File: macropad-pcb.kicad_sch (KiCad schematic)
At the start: 25 parts, among them J1 Conn_01x01_Socket, J10 Conn_01x01_Socket, J2 Conn_01x01_Socket, J3 Conn_01x01_Socket, J4 Conn_01x01_Socket, J5 Conn_01x01_Socket, J6 Conn_01x01_Socket, J7 Conn_01x01_Socket, J8 Conn_01x01_Socket, J9 Conn_01x01_Socket

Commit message: updated w. flipped main connectior
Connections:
- net GND: now also MAIN1.1, MAIN1.2, MAIN1.3, MAIN1.4; no longer MAIN1.13, MAIN1.14, MAIN1.15, MAIN1.16
- net LED_DI: now also MAIN1.6; no longer MAIN1.11
- net LED_DO_MACRO: now also MAIN1.5; no longer MAIN1.12
- net VCC: now also MAIN1.13, MAIN1.14, MAIN1.15, MAIN1.16; no longer MAIN1.1, MAIN1.2, MAIN1.3, MAIN1.4
- net col10: now also MAIN1.10; no longer MAIN1.7
- net col11: now also MAIN1.9; no longer MAIN1.8
- net col8: now also MAIN1.12; no longer MAIN1.5
- net col9: now also MAIN1.11; no longer MAIN1.6
- net row8: now also MAIN1.8; no longer MAIN1.9
- net row9: now also MAIN1.7; no longer MAIN1.10

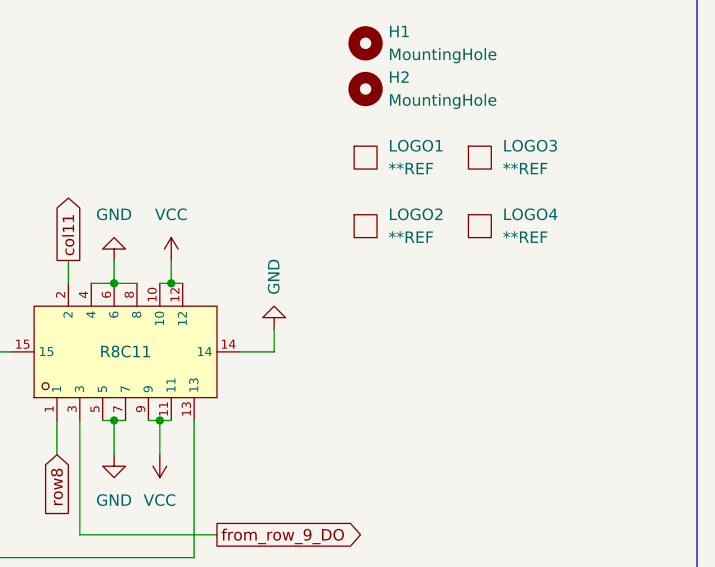
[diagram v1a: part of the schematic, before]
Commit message: added cyboard logo
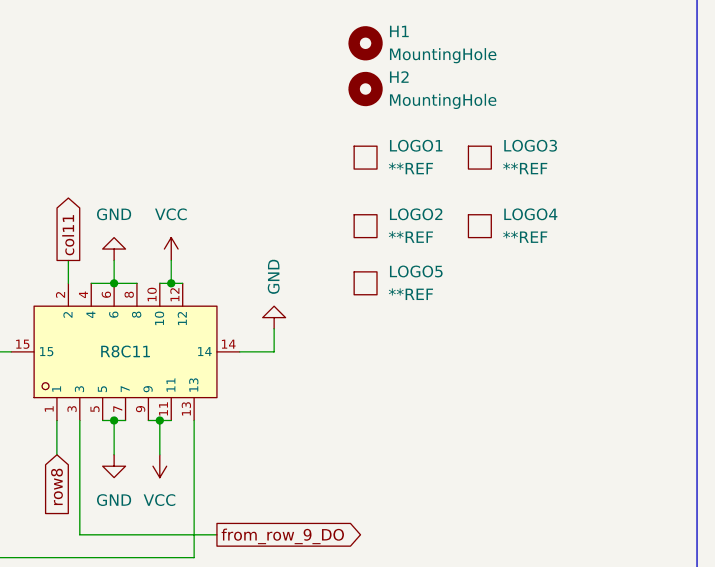
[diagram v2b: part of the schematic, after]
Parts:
- added LOGO5: **REF, ct-kicad:cyboard-logo-10mm, symbol ct-kicad:cyboard-logo-10mm
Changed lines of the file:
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@@
+    )
+  )
+  (symbol (lib_id "ct-kicad:cyboard-logo-10mm") (at 240.03 72.39 0) (unit 1)
+    (in_bom no) (on_board yes) (dnp no) (fields_autoplaced)
+    (property "Reference" "LOGO5" (at 242.57 71.12 0)
+      (effects (font (size 1.27 1.27)) (justify left))
+    )
+    (property "Value" "**REF" (at 242.57 73.66 0)
+      (effects (font (size 1.27 1.27)) (justify left))
+    )
+    (property "Footprint" "ct-kicad:cyboard-logo-10mm" (at 240.03 72.39 0)
+      (effects (font (size 1.27 1.27)) hide)
+    )
+    (property "Datasheet" "" (at 240.03 72.39 0)
+      (effects (font (size 1.27 1.27)) hide)
+    )
+    (instances
+      (project "macropad-pcb"
+        (path "/a1d63ebf-3d6e-4f37-a8f0-07094ad9e2ad"
+          (reference "LOGO5") (unit 1)
+        )
+      )
     )
   )

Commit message: added cyboard logo, placed order
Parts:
- H1, H2, J1, J2, J3, J4, J5, J6, J7, J8: now left out of the parts list
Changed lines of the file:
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@@
   )
   (symbol (lib_id "Connector:Conn_01x01_Socket") (at 30.48 142.24 180) (unit 1)
-    (in_bom yes) (on_board yes) (dnp no) (fields_autoplaced)
+    (in_bom no) (on_board yes) (dnp no) (fields_autoplaced)
     (property "Reference" "J3" (at 31.115 137.16 0)
       (effects (font (size 1.27 1.27)))
@@
   )
   (symbol (lib_id "Connector:Conn_01x01_Socket") (at 30.48 134.62 180) (unit 1)
-    (in_bom yes) (on_board yes) (dnp no) (fields_autoplaced)
+    (in_bom no) (on_board yes) (dnp no) (fields_autoplaced)
     (property "Reference" "J2" (at 31.115 129.54 0)
       (effects (font (size 1.27 1.27)))
@@
   )
   (symbol (lib_id "Mechanical:MountingHole") (at 240.03 50.8 0) (unit 1)
-    (in_bom yes) (on_board yes) (dnp no) (fields_autoplaced)
+    (in_bom no) (on_board yes) (dnp no) (fields_autoplaced)
     (property "Reference" "H2" (at 242.57 49.53 0)
       (effects (font (size 1.27 1.27)) (justify left))
@@
   )
   (symbol (lib_id "Connector:Conn_01x01_Socket") (at 57.15 128.27 180) (unit 1)
-    (in_bom yes) (on_board yes) (dnp no) (fields_autoplaced)
+    (in_bom no) (on_board yes) (dnp no) (fields_autoplaced)
     (property "Reference" "J5" (at 57.785 123.19 0)
       (effects (font (size 1.27 1.27)))
@@
   )
   (symbol (lib_id "Connector:Conn_01x01_Socket") (at 57.15 135.89 180) (unit 1)
-    (in_bom yes) (on_board yes) (dnp no) (fields_autoplaced)
+    (in_bom no) (on_board yes) (dnp no) (fields_autoplaced)
     (property "Reference" "J6" (at 57.785 130.81 0)
       (effects (font (size 1.27 1.27)))
@@
   )
   (symbol (lib_id "Connector:Conn_01x01_Socket") (at 57.15 151.13 180) (unit 1)
-    (in_bom yes) (on_board yes) (dnp no) (fields_autoplaced)
+    (in_bom no) (on_board yes) (dnp no) (fields_autoplaced)
     (property "Reference" "J8" (at 57.785 146.05 0)
       (effects (font (size 1.27 1.27)))
@@
   )
   (symbol (lib_id "Mechanical:MountingHole") (at 240.03 45.72 0) (unit 1)
-    (in_bom yes) (on_board yes) (dnp no) (fields_autoplaced)
+    (in_bom no) (on_board yes) (dnp no) (fields_autoplaced)
     (property "Reference" "H1" (at 242.57 44.45 0)
       (effects (font (size 1.27 1.27)) (justify left))
@@
   )
   (symbol (lib_id "Connector:Conn_01x01_Socket") (at 30.48 149.86 180) (unit 1)
-    (in_bom yes) (on_board yes) (dnp no) (fields_autoplaced)
+    (in_bom no) (on_board yes) (dnp no) (fields_autoplaced)
     (property "Reference" "J4" (at 31.115 144.78 0)
       (effects (font (size 1.27 1.27)))
@@
   )
   (symbol (lib_id "Connector:Conn_01x01_Socket") (at 57.15 143.51 180) (unit 1)
-    (in_bom yes) (on_board yes) (dnp no) (fields_autoplaced)
+    (in_bom no) (on_board yes) (dnp no) (fields_autoplaced)
     (property "Reference" "J7" (at 57.785 138.43 0)
       (effects (font (size 1.27 1.27)))
@@
   )
   (symbol (lib_id "Connector:Conn_01x01_Socket") (at 30.48 127 180) (unit 1)
-    (in_bom yes) (on_board yes) (dnp no) (fields_autoplaced)
+    (in_bom no) (on_board yes) (dnp no) (fields_autoplaced)
     (property "Reference" "J1" (at 31.115 121.92 0)
       (effects (font (size 1.27 1.27)))
